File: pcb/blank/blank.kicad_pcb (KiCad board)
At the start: 2 copper layers, 6 parts

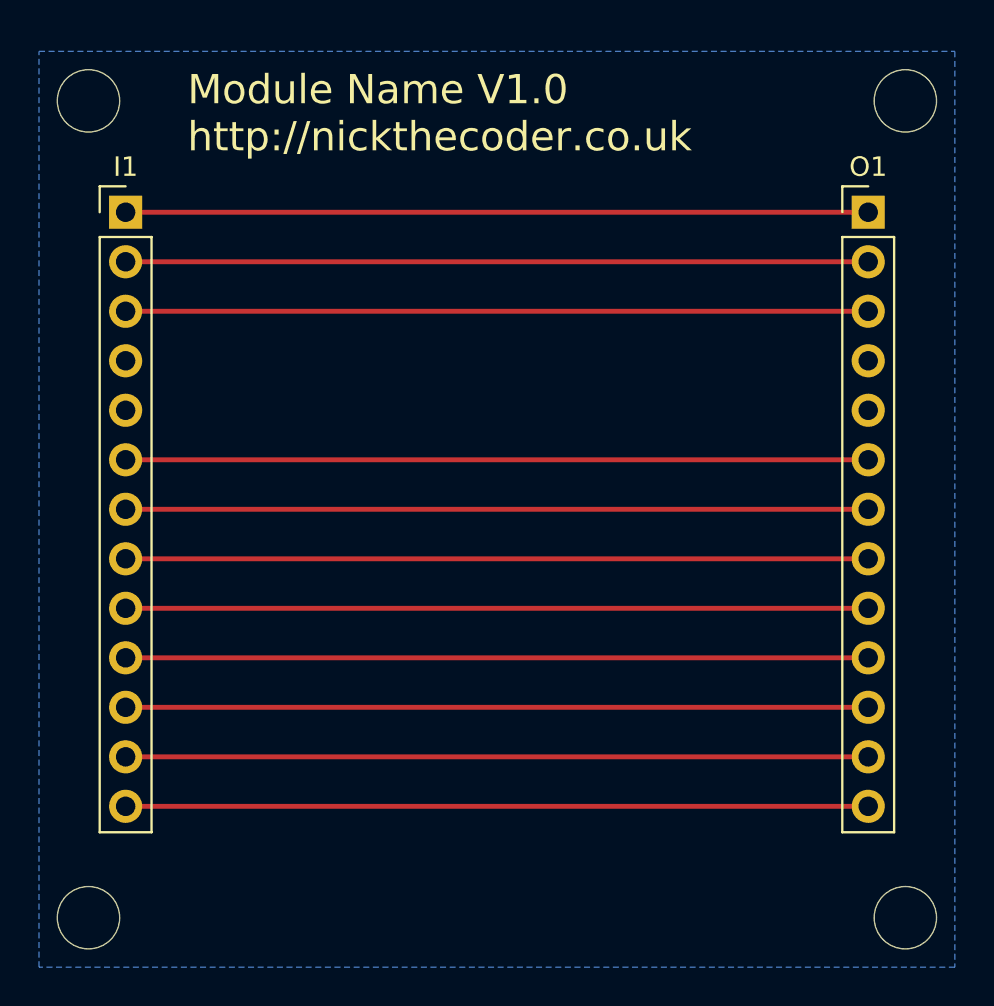
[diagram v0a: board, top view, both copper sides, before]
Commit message: Added a new "power" and LEDs module (split into two half size modules)
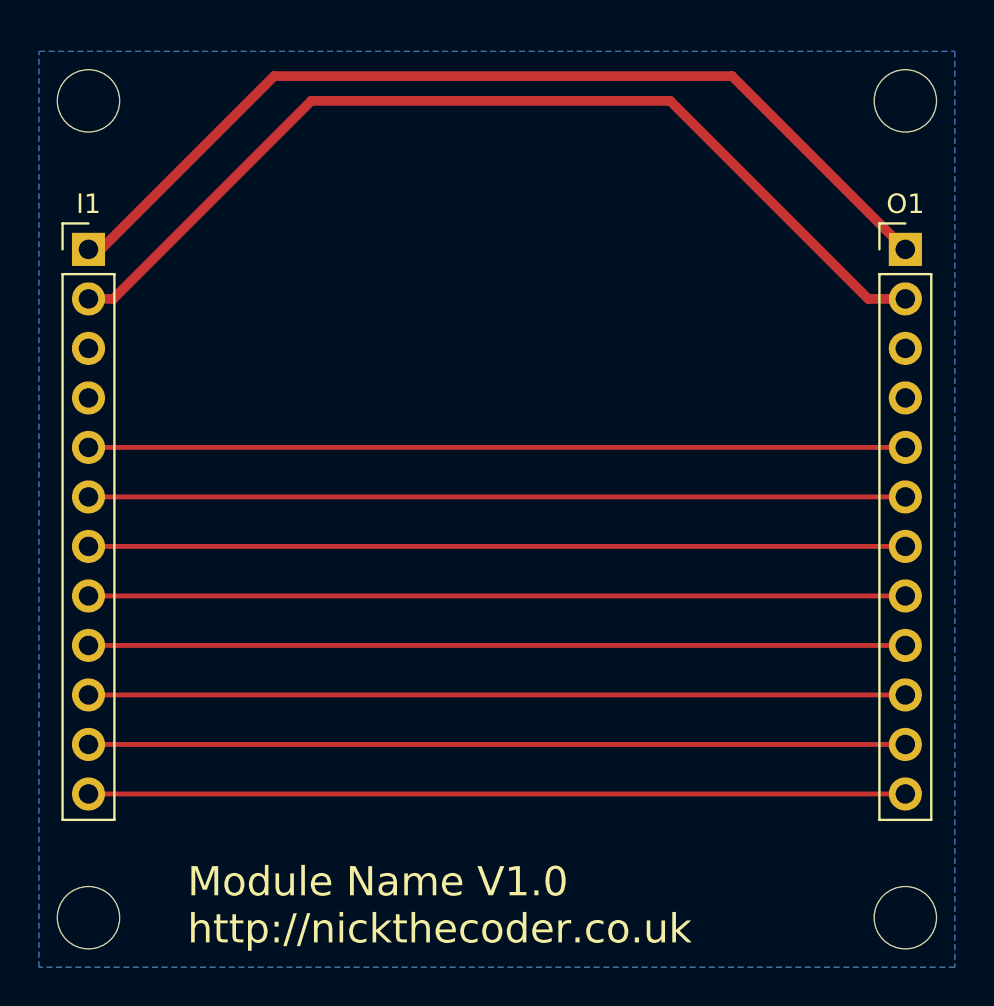
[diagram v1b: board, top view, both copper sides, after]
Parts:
- I1: value ePlayInput -> Input; footprint Pin_Headers:Pin_Header_Straight_1x13_Pitch2.54mm -> Pin_Headers:Pin_Header_Straight_1x12_Pitch2.54mm
- O1: value ePlayOutput -> Output; footprint Socket_Strips:Socket_Strip_Straight_1x13_Pitch2.54mm -> Socket_Strips:Socket_Strip_Straight_1x12_Pitch2.54mm
- moved I1 2.69 mm to (128.3, 94.0)
- moved O1 2.69 mm to (170.2, 94.0)
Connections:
- I1 pad 10: /L4 -> /L5
- I1 pad 11: /L5 -> /L6
- I1 pad 12: /L6 -> /L7
- I1 pad 3: /3V3 -> Earth
- I1 pad 4: Earth -> (no net)
- I1 pad 5: (no net) -> /L0
- I1 pad 6: /L0 -> /L1
- I1 pad 7: /L1 -> /L2
- I1 pad 8: /L2 -> /L3
- I1 pad 9: /L3 -> /L4
- O1 pad 10: /L4 -> /L5
- O1 pad 11: /L5 -> /L6
- O1 pad 12: /L6 -> /L7
- O1 pad 3: /3V3 -> Earth
- O1 pad 4: Earth -> (no net)
- O1 pad 5: (no net) -> /L0
- O1 pad 6: /L0 -> /L1
- O1 pad 7: /L1 -> /L2
- O1 pad 8: /L2 -> /L3
- O1 pad 9: /L3 -> /L4
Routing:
- net /3V3: track 38.1 -> 0.00 mm
- net /VCC: track 38.1 -> 50.3 mm
- net /VIN: track 38.1 -> 49.3 mm
- net /L7: track 38.1 -> 41.9 mm
- net /L6: track 38.1 -> 41.9 mm
- net /L5: track 38.1 -> 41.9 mm
- net /L4: track 38.1 -> 41.9 mm
- net /L3: track 38.1 -> 41.9 mm
- net /L2: track 38.1 -> 41.9 mm
- net /L1: track 38.1 -> 41.9 mm
- net /L0: track 38.1 -> 41.9 mm

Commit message: Tidied up blank, and removed the voltage regulator from "power" module.
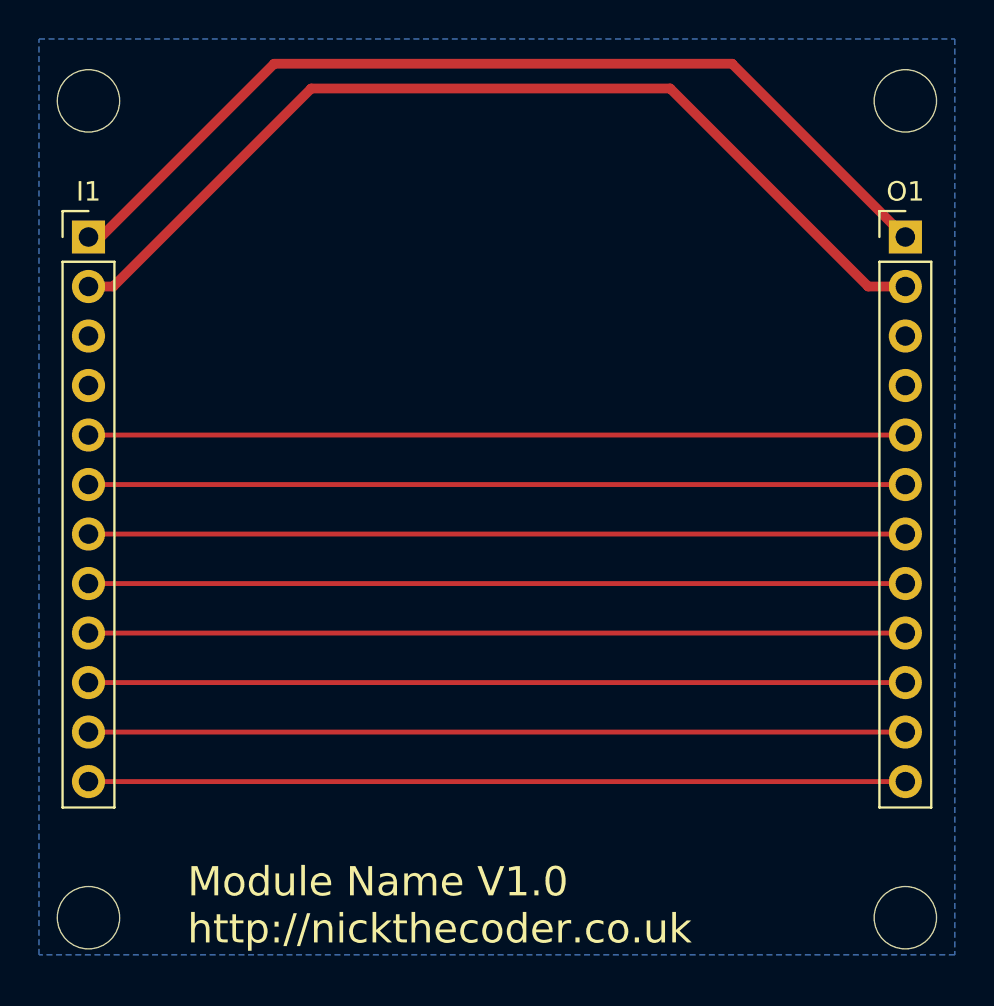
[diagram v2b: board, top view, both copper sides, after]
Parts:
- moved I1 0.64 mm to (128.3, 93.3)
- moved O1 0.64 mm to (170.2, 93.3)
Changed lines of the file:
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@@
     (links 11)
     (no_connects 0)
-    (area 0 0 0 0)
+    (area 124.46 82.55 173.990001 132.080001)
     (thickness 1.6)
     (drawings 1)
@@
     (descr "Mounting Hole 3.2mm, no annular, M3")
     (tags "mounting hole 3.2mm no annular m3")
-    (fp_text reference M3 (at 3.175 0) (layer F.Fab)
+    (fp_text reference M3 (at 0 2.54) (layer F.Fab)
       (effects (font (size 1 1) (thickness 0.15)))
     )
@@
     (descr "Mounting Hole 3.2mm, no annular, M3")
     (tags "mounting hole 3.2mm no annular m3")
-    (fp_text reference M3 (at -3.175 0) (layer F.Fab)
+    (fp_text reference M3 (at 0 2.54) (layer F.Fab)
       (effects (font (size 1 1) (thickness 0.15)))
     )
@@
       (effects (font (size 1 1) (thickness 0.15)))
     )
-    (fp_text value M3 (at -3.175 0) (layer F.Fab)
+    (fp_text value M3 (at 0 -2.54) (layer F.Fab)
       (effects (font (size 1 1) (thickness 0.15)))
     )
@@
       (effects (font (size 1 1) (thickness 0.15)))
     )
-    (fp_text value M3 (at 3.175 0) (layer F.Fab)
+    (fp_text value M3 (at 0 -2.54) (layer F.Fab)
       (effects (font (size 1 1) (thickness 0.15)))
     )
@@
   )
   (module Pin_Headers:Pin_Header_Straight_1x12_Pitch2.54mm (layer F.Cu)
-    (at 128.27 93.98)
+    (at 128.27 93.345)
     (descr "Through hole straight pin header, 1x12, 2.54mm pitch, single row")
     (tags "Through hole pin header THT 1x12 2.54mm single row")
@@
   )
   (module Socket_Strips:Socket_Strip_Straight_1x12_Pitch2.54mm (layer F.Cu)
-    (at 170.18 93.98)
+    (at 170.18 93.345)
     (descr "Through hole straight socket strip, 1x12, 2.54mm pitch, single row")
     (tags "Through hole socket strip THT 1x12 2.54mm single row")
@@
     (effects (font (size 1.5 1.5) (thickness 0.3)) (justify left))
   )
-  (segment (start 128.27 93.98) (end 128.905 93.98) (width 0.5) (layer F.Cu) (net 1) (status C00000))
-  (segment (start 128.905 93.98) (end 137.795 85.09) (width 0.5) (layer F.Cu) (net 1) (status 400000))
-  (segment (start 170.18 93.98) (end 161.29 85.09) (width 0.5) (layer F.Cu) (net 1) (status 400000))
-  (segment (start 161.29 85.09) (end 137.795 85.09) (width 0.5) (layer F.Cu) (net 1))
-  (segment (start 128.27 96.52) (end 129.54 96.52) (width 0.5) (layer F.Cu) (net 2) (status 400000))
-  (segment (start 168.275 96.52) (end 170.18 96.52) (width 0.5) (layer F.Cu) (net 2) (status 800000))
-  (segment (start 158.115 86.36) (end 168.275 96.52) (width 0.5) (layer F.Cu) (net 2))
-  (segment (start 139.7 86.36) (end 158.115 86.36) (width 0.5) (layer F.Cu) (net 2))
-  (segment (start 129.54 96.52) (end 139.7 86.36) (width 0.5) (layer F.Cu) (net 2))
-  (segment (start 128.27 104.14) (end 170.18 104.14) (width 0.25) (layer F.Cu) (net 4) (status C00000))
-  (segment (start 128.27 106.68) (end 170.18 106.68) (width 0.25) (layer F.Cu) (net 5) (status C00000))
-  (segment (start 170.18 109.22) (end 128.27 109.22) (width 0.25) (layer F.Cu) (net 6) (status C00000))
-  (segment (start 128.27 111.76) (end 170.18 111.76) (width 0.25) (layer F.Cu) (net 7) (status C00000))
-  (segment (start 170.18 114.3) (end 128.27 114.3) (width 0.25) (layer F.Cu) (net 8) (status C00000))
-  (segment (start 128.27 116.84) (end 170.18 116.84) (width 0.25) (layer F.Cu) (net 9) (status C00000))
-  (segment (start 170.18 119.38) (end 128.27 119.38) (width 0.25) (layer F.Cu) (net 10) (status C00000))
-  (segment (start 128.27 121.92) (end 170.18 121.92) (width 0.25) (layer F.Cu) (net 11) (status C00000))
+  (segment (start 161.29 84.455) (end 137.795 84.455) (width 0.5) (layer F.Cu) (net 1))
+  (segment (start 128.27 93.345) (end 128.905 93.345) (width 0.5) (layer F.Cu) (net 1))
+  (segment (start 128.905 93.345) (end 137.795 84.455) (width 0.5) (layer F.Cu) (net 1))
+  (segment (start 170.18 93.345) (end 161.29 84.455) (width 0.5) (layer F.Cu) (net 1))
+  (segment (start 139.7 85.725) (end 158.115 85.725) (width 0.5) (layer F.Cu) (net 2))
+  (segment (start 128.27 95.885) (end 129.54 95.885) (width 0.5) (layer F.Cu) (net 2))
+  (segment (start 168.275 95.885) (end 170.18 95.885) (width 0.5) (layer F.Cu) (net 2))
+  (segment (start 158.115 85.725) (end 168.275 95.885) (width 0.5) (layer F.Cu) (net 2))
+  (segment (start 129.54 95.885) (end 139.7 85.725) (width 0.5) (layer F.Cu) (net 2))
+  (segment (start 128.27 103.505) (end 170.18 103.505) (width 0.25) (layer F.Cu) (net 4))
+  (segment (start 128.27 106.045) (end 170.18 106.045) (width 0.25) (layer F.Cu) (net 5))
+  (segment (start 170.18 108.585) (end 128.27 108.585) (width 0.25) (layer F.Cu) (net 6))
+  (segment (start 128.27 111.125) (end 170.18 111.125) (width 0.25) (layer F.Cu) (net 7))
+  (segment (start 170.18 113.665) (end 128.27 113.665) (width 0.25) (layer F.Cu) (net 8))
+  (segment (start 128.27 116.205) (end 170.18 116.205) (width 0.25) (layer F.Cu) (net 9))
+  (segment (start 170.18 118.745) (end 128.27 118.745) (width 0.25) (layer F.Cu) (net 10))
+  (segment (start 128.27 121.285) (end 170.18 121.285) (width 0.25) (layer F.Cu) (net 11))
   (zone (net 0) (net_name "") (layer Edge.Cuts) (hatch edge 0.508)
     (connect_pads (clearance 0.508))
@@
     (polygon
       (pts
-        (xy 172.72 130.81) (xy 125.73 130.81) (xy 125.73 83.82) (xy 172.72 83.82)
+        (xy 172.72 130.175) (xy 125.73 130.175) (xy 125.73 83.185) (xy 172.72 83.185)
       )
     )
